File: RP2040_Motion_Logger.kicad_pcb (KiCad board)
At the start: 4 copper layers, 22.9 x 63 mm, 68 parts, among them J1 Conn_01x02, J2 Conn_01x14, J3 TC2030-NL, J4 Micro_SD_Card_Det1, J5 Conn_01x14, J6 Conn_01x02, P1 USB_C_Plug_USB2.0, Q1 AO3401A, SW1 RESET, U1 RP2040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

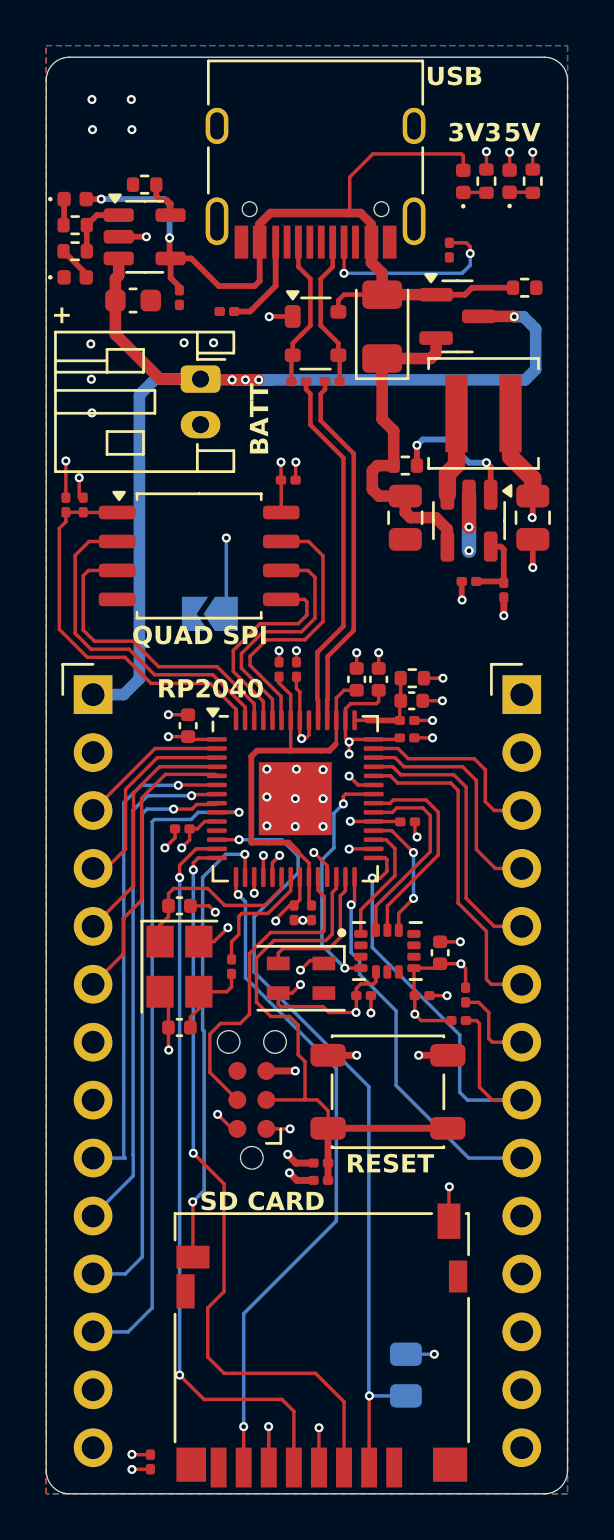
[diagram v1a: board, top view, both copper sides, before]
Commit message: Added a bootloader button and made some other QOL changes... mostly aesthetic.
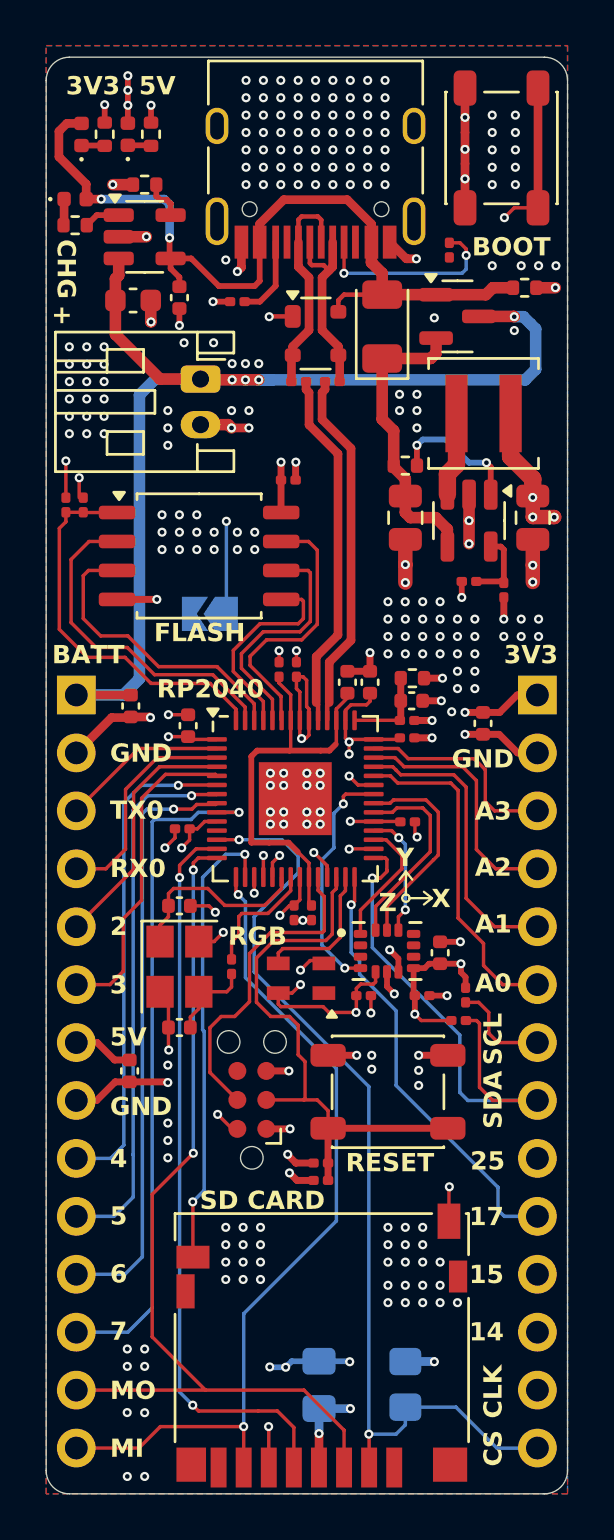
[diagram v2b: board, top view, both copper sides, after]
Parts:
- removed D3: Green, LED_SMD:LED_0402_1005Metric
- removed R9: 5K, Resistor_SMD:R_0402_1005Metric
- added C10: 1u, Capacitor_SMD:C_0402_1005Metric, F.Cu at (179.4, 112.5)
- added C27: 1u, Capacitor_SMD:C_0402_1005Metric, F.Cu at (194.9, 97.3)
- added C9: 1u, Capacitor_SMD:C_0402_1005Metric, F.Cu at (179.5, 96.5)
- added SW2: BOOTLOADER, Button_Switch_SMD:SW_SPST_PTS647_Sx38, F.Cu at (195.7, 72.1)
- C18: value 100n -> 4u7; footprint Capacitor_SMD:C_0201_0603Metric -> Capacitor_SMD:C_0402_1005Metric
- C26: footprint Capacitor_SMD:C_0201_0603Metric -> Capacitor_SMD:C_0805_2012Metric_Pad1.18x1.45mm_HandSolder; moved to B.Cu
- R15: footprint Resistor_SMD:R_0805_2012Metric -> Resistor_SMD:R_0805_2012Metric_Pad1.20x1.40mm_HandSolder
- moved D7 16.9 mm to (177.3, 71.5)
- moved R17 16.9 mm to (180.4, 71.5)
- moved D6 16.9 mm to (179.3, 71.5)
- moved R20 16.9 mm to (178.3, 71.5)
- moved C26 8.13 mm to (187.7, 126.3)
- moved J2 0.74 mm to (177.1, 96.0)
- moved J5 0.69 mm to (197.3, 96.0)
- moved R3 0.63 mm to (184.2, 78.8)
- moved C16 0.43 mm to (189.0, 95.5)
- moved R15 0.41 mm to (191.5, 126.3)
- moved C15 0.40 mm to (190.0, 95.5)
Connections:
- net GPIO_0 renamed MCU_TX0
- net GPIO_1 renamed MCU_RX0
- net MCU_RX renamed GPIO_ADC3
- net MCU_TX renamed GPIO_ADC2
- J2 pad 13: +3V3 -> SD_MOSI
- J2 pad 14: GND -> SD_MISO
- J5 pad 10: GPIO_25 -> GPIO_17
- J5 pad 13: +3V3 -> SD_CLK
- J5 pad 14: GND -> SD_nCS
- J5 pad 9: GPIO_17 -> GPIO_25
- P1 pad A6: (no net) -> /USB_D+
- P1 pad A7: (no net) -> /USB_D-
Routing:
- net GND: track 36.4 -> 71.5 mm, vias 53 -> 280
- net /Sensors & Peripherals/usb_boot: track 14.3 -> 41.2 mm, vias 2 -> 3
- net SD_CLK: track 32.4 -> 47.8 mm
- net +3V3: track 50.6 -> 59.1 mm, vias 22 -> 27
- net SD_MISO: track 29.4 -> 37.1 mm
- net SD_nCS: track 35.2 -> 42.6 mm
- net SD_MOSI: track 33.3 -> 40.1 mm
- net +BATT: track 46.8 -> 49.9 mm
- net /USB_D+: track 6.68 -> 9.71 mm
- net GPIO_17: track 16.8 -> 19.2 mm
- net GPIO_25: track 27.8 -> 25.5 mm
- net Net-(D5-K): track 15.1 -> 13.2 mm
- net /USB_D-: track 6.68 -> 8.53 mm
- net Net-(D3-A): track 1.56 -> 0.00 mm
- net GPIO_SDA1: track 21.3 -> 22.7 mm
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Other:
- board text added: "BOOT"
- board text added: "CHG"
- board text added: "CLK"
- board text added: "CS"
- board text added: "FLASH"
- board text added: "MI"
- board text added: "MO"
- board text added: "RGB"
- board text added: "RX0"
- board text added: "SCL"
- board text added: "SDA"
- board text added: "TX0"
- board text added: "X"
- board text added: "Y"
- board text added: "Z"
- board text removed: "0"
- board text removed: "1"
- board text removed: "BATT +"
- board text removed: "QUAD SPI"
- board text removed: "SCL1"
- board text removed: "SDA1"
- board text removed: "USB"
- board text removed: "VBUS"

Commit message: removed the DNF silkscreen for the SD Card connector's CS pin pullup resistor
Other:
- board text removed: "DNF"
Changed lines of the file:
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@@
-		)
-	)
-	(gr_text "DNF"
-		(at 192.8114 124.0536 0)
-		(layer "B.SilkS")
-		(effects
-			(font
-				(size 0.8001 0.8001)
-				(thickness 0.1524)
-				(bold yes)
-			)
-			(justify left bottom mirror)
 		)
 	)
